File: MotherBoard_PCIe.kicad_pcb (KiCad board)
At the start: 2 copper layers, 90 x 100 mm, 27 parts, among them J1 Conn_01x02, J2 Conn_01x07, J3 Conn_01x02, J4 Conn_01x07, J5 Bus_PCIexpress_x16_164_Positi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, J6 Bus_PCIexpress_x16_164_Positi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, J7 Bus_PCIexpress_x16_164_Positi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, J8 Bus_PCIexpress_x16_164_Positi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, J9 Bus_mechaken_PCIexpress_x16_1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

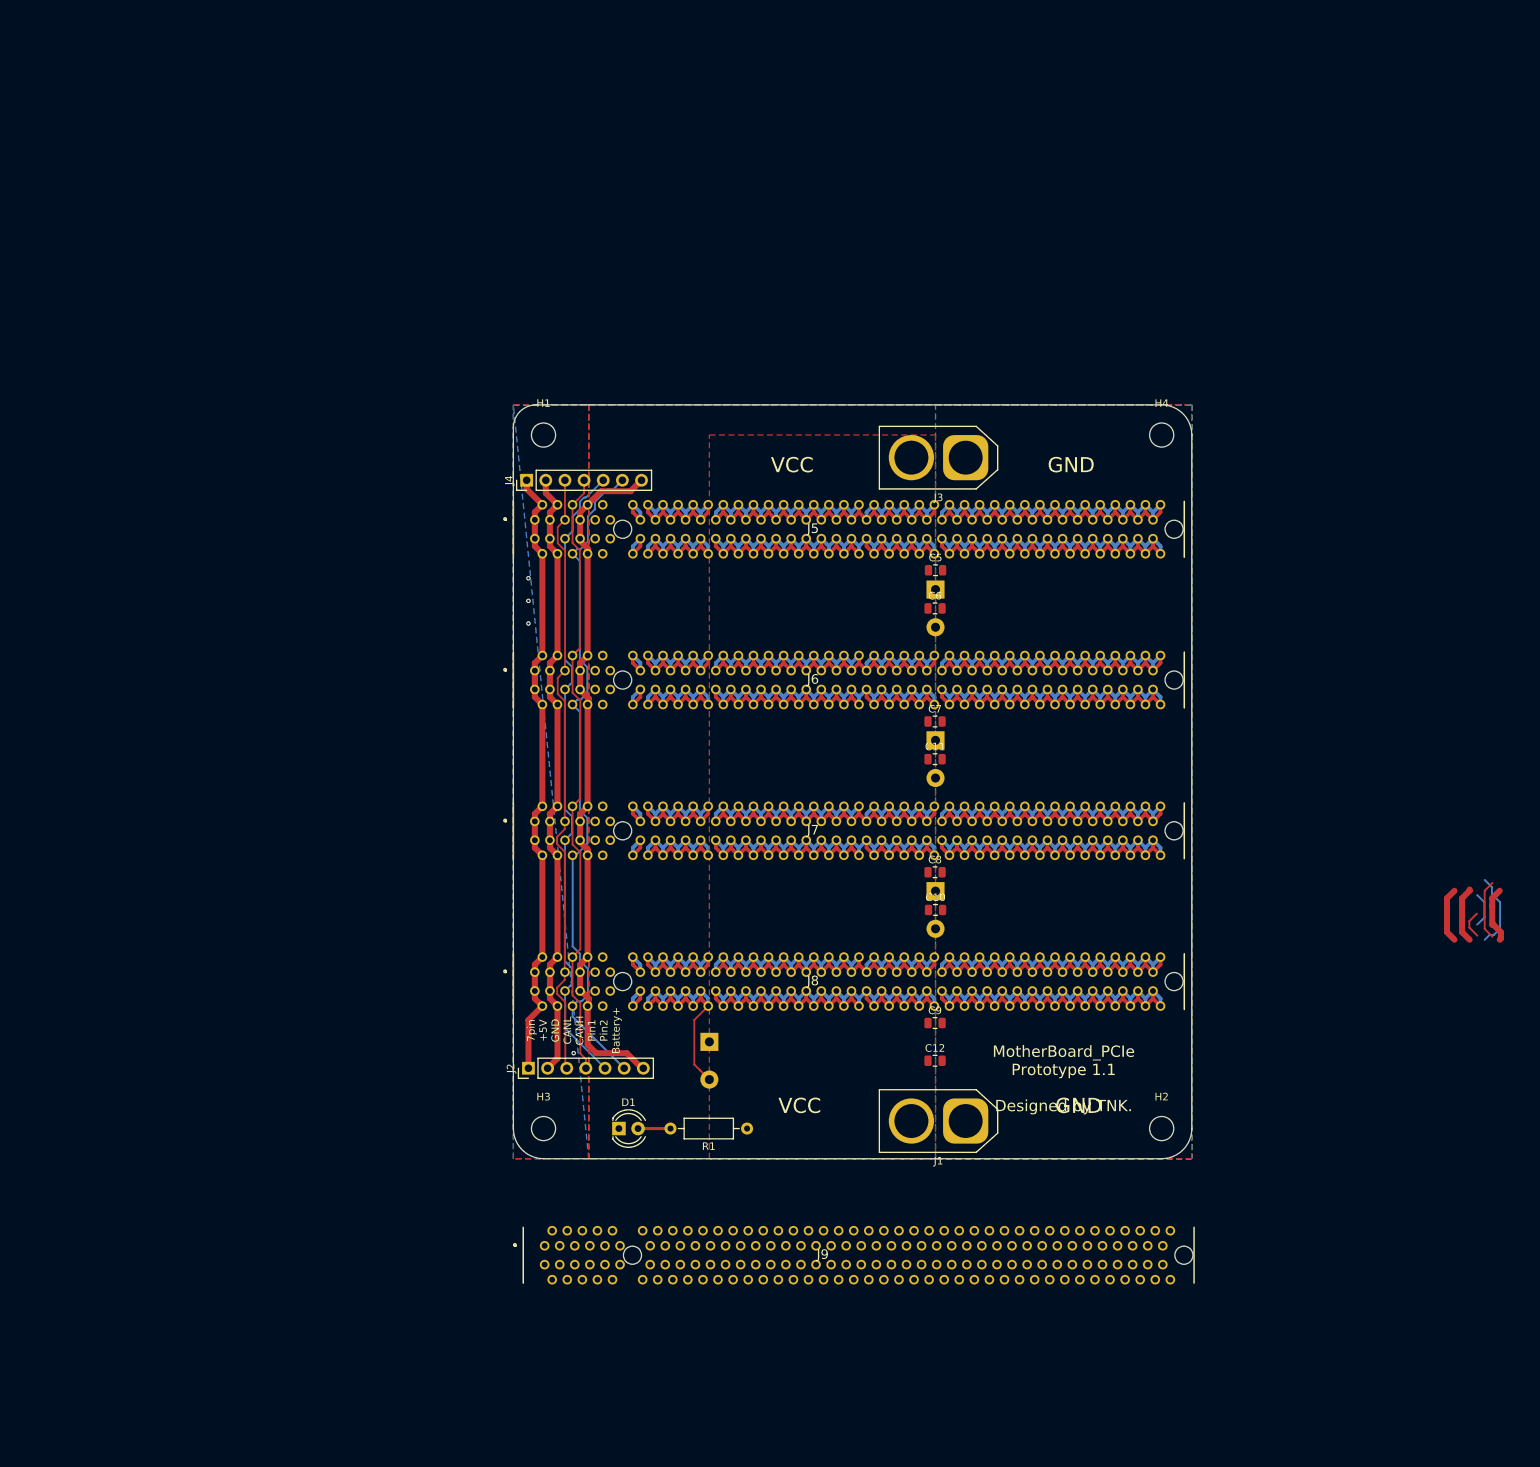
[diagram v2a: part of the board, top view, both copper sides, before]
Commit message: change
おおよその部品の配置を開始
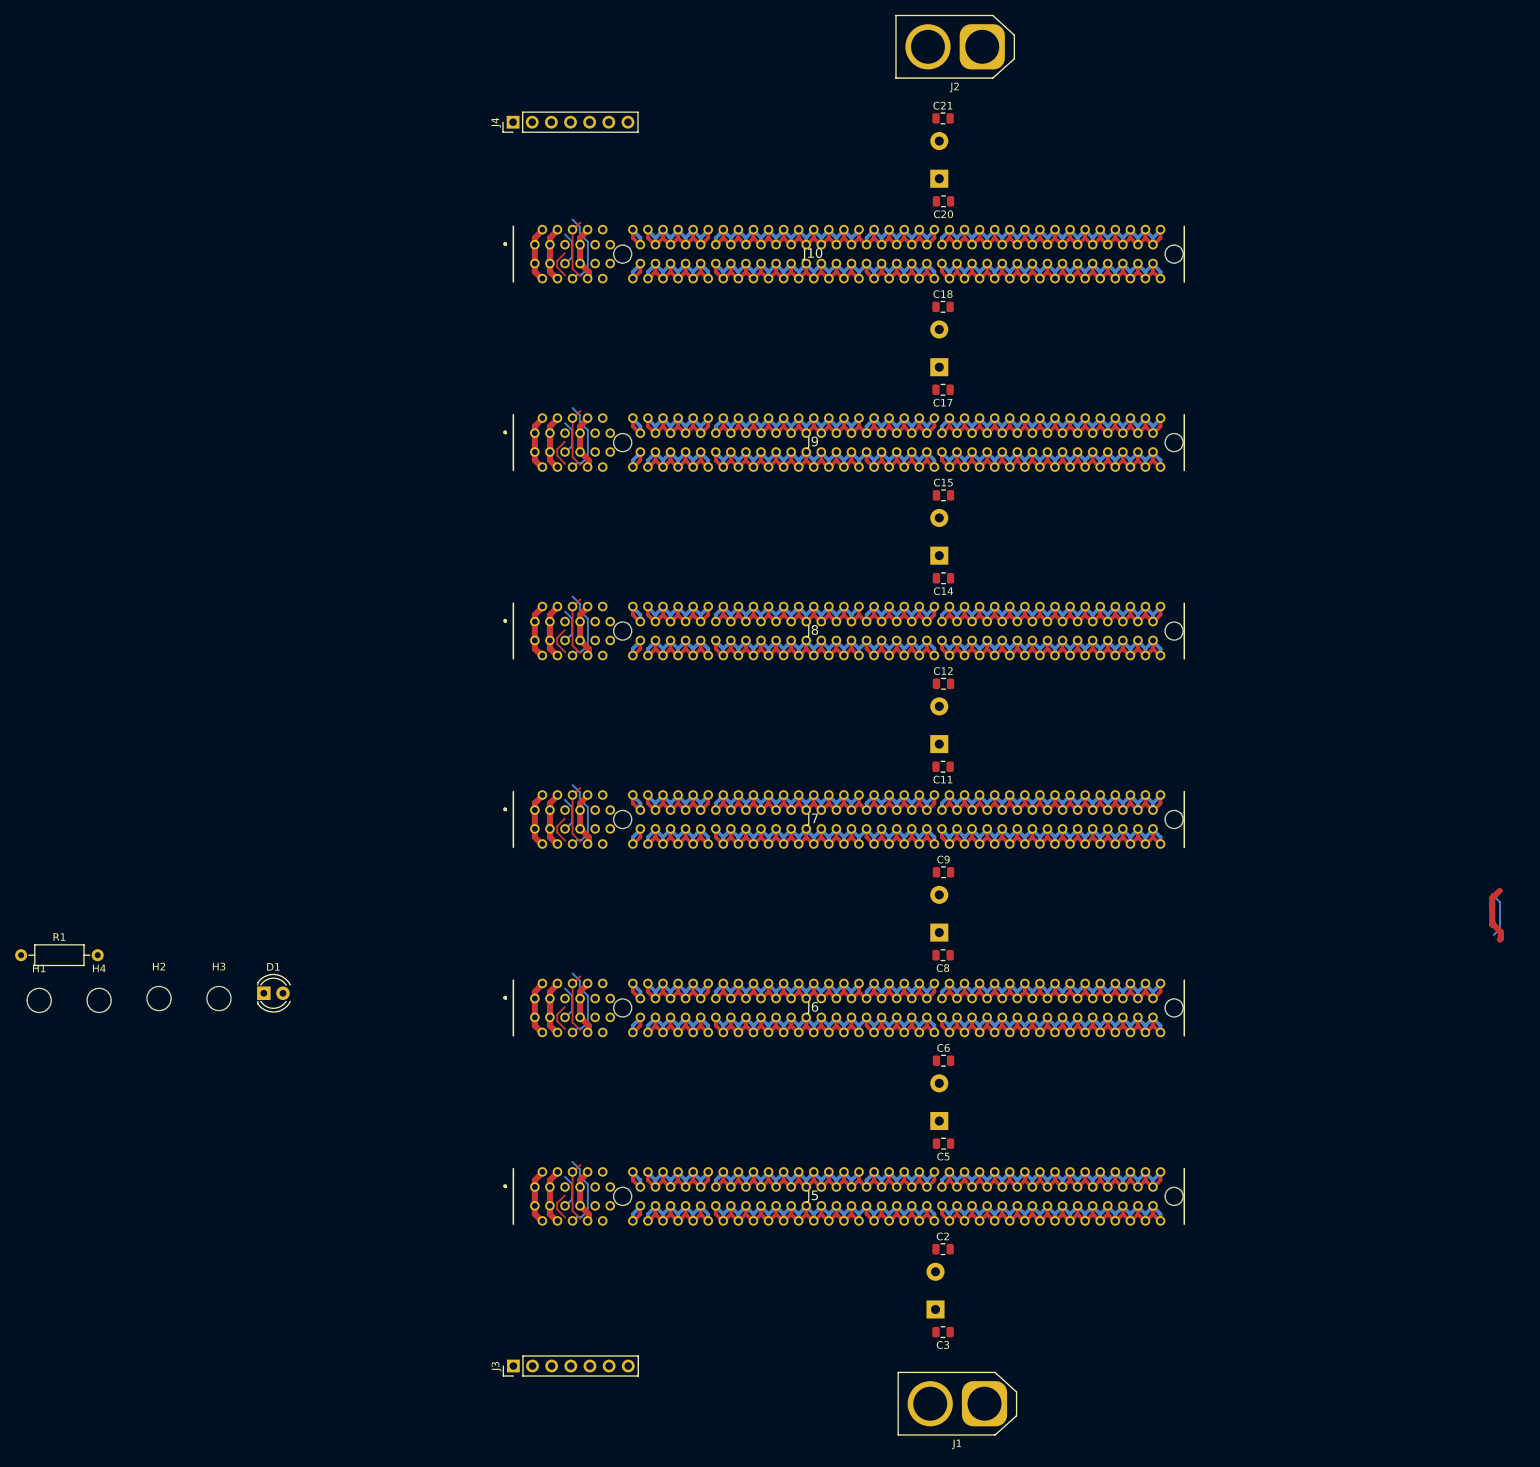
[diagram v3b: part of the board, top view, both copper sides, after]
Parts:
- added C13: 1000uF, Capacitor_THT:CP_Radial_D12.5mm_P5.00mm, B.Cu at (146.5, 85.0)
- added C14: 1uF, Capacitor_SMD:C_0805_2012Metric, F.Cu at (147.1, 88.0)
- added C15: 10uF, Capacitor_SMD:C_0805_2012Metric, F.Cu at (147.1, 77.0)
- added C16: 1000uF, Capacitor_THT:CP_Radial_D12.5mm_P5.00mm, B.Cu at (146.5, 60.0)
- added C17: 1uF, Capacitor_SMD:C_0805_2012Metric, F.Cu at (147.0, 63.0)
- added C18: 10uF, Capacitor_SMD:C_0805_2012Metric, F.Cu at (147.0, 52.0)
- added C19: 1000uF, Capacitor_THT:CP_Radial_D12.5mm_P5.00mm, B.Cu at (146.5, 35.0)
- added C20: 1uF, Capacitor_SMD:C_0805_2012Metric, F.Cu at (147.1, 38.0)
- added C21: 10uF, Capacitor_SMD:C_0805_2012Metric, F.Cu at (147.0, 27.0)
- added J10: Bus_mechaken_PCIexpress_x16_164_Position, PCIe:Socket_mechaken_PCIexpress_x16_164_position, F.Cu at (90.0, 45.0)
- C10: value 10uF -> 1000uF; footprint Capacitor_SMD:C_0805_2012Metric -> Capacitor_THT:CP_Radial_D12.5mm_P5.00mm; moved to B.Cu
- C11: value 10uF -> 1uF
- C2: value 1000uF -> 1uF; footprint Capacitor_THT:CP_Radial_D12.5mm_P5.00mm -> Capacitor_SMD:C_0805_2012Metric; moved to F.Cu
- C3: value 1000uF -> 10uF; footprint Capacitor_THT:CP_Radial_D12.5mm_P5.00mm -> Capacitor_SMD:C_0805_2012Metric; moved to F.Cu
- C7: value 1uF -> 1000uF; footprint Capacitor_SMD:C_0805_2012Metric -> Capacitor_THT:CP_Radial_D12.5mm_P5.00mm; moved to B.Cu
- C9: value 1uF -> 10uF
- J1: footprint Connector_AMASS:AMASS_XT60-F_1x02_P7.20mm_Vertical -> Connector_AMASS:AMASS_XT60-M_1x02_P7.20mm_Vertical
- J2: value Conn_01x07 -> Conn_01x02; footprint Connector_PinHeader_2.54mm:PinHeader_1x07_P2.54mm_Vertical -> Connector_AMASS:AMASS_XT60-F_1x02_P7.20mm_Vertical
- J3: value Conn_01x02 -> Conn_01x07; footprint Connector_AMASS:AMASS_XT60-M_1x02_P7.20mm_Vertical -> Connector_PinHeader_2.54mm:PinHeader_1x07_P2.54mm_Vertical
- J5, J6, J7, J8: value Bus_PCIexpress_x16_164_Position -> Bus_mechaken_PCIexpress_x16_164_Position; footprint SamacSys_Parts:10018783-10113TLF -> PCIe:Socket_mechaken_PCIexpress_x16_164_position
- moved H4 159.7 mm to (35.0, 144.0)
- moved J2 148.3 mm to (152.2, 17.5), turned to 180 degrees
- moved J3 134.6 mm to (90.0, 192.5), turned to 90 degrees
- moved H2 134.1 mm to (43.0, 143.8)
- moved J9 107.8 mm to (90.0, 70.0)
- moved H1 100.5 mm to (27.1, 144.0)
- moved R1 99.0 mm to (24.7, 138.0), turned to 0 degrees
- moved C3 98.5 mm to (147.0, 188.0), turned to 0 degrees
- moved J5 88.5 mm to (90.0, 170.0)
- moved C5 76.1 mm to (147.1, 163.0)
- moved C2 67.5 mm to (147.0, 177.0), turned to 0 degrees
- moved C6 60.0 mm to (147.1, 152.0)
- moved C1 55.5 mm to (146.0, 185.0), turned to 90 degrees
- moved D1 50.4 mm to (56.9, 143.1)
- moved C12 50.0 mm to (147.1, 102.0)
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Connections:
- J2 pad 1: +5V -> GNDPWR
- J2 pad 2: GND -> VCC
- J3 pad 1: GNDPWR -> +5V
- J3 pad 2: VCC -> GND
- J5 pad A10: VCC -> GNDPWR
- J5 pad A2: +5V -> GND
- J5 pad A3: GND -> CANL
- J5 pad A4: GND -> CANH
- J5 pad A5: CANL -> +BATT
- J5 pad A6: CANH -> VCC
- J5 pad A7: +BATT -> VCC
- J5 pad A8: +BATT -> GNDPWR
- J5 pad B10: VCC -> GNDPWR
- J5 pad B2: +5V -> GND
- J5 pad B3: GND -> Pin_B5
- J5 pad B4: GND -> Pin_B6
- J5 pad B5: Pin_B5 -> +BATT
- J5 pad B6: Pin_B6 -> VCC
- J5 pad B7: +BATT -> VCC
- J5 pad B8: +BATT -> GNDPWR
- J6 pad A10: VCC -> GNDPWR
- J6 pad A2: +5V -> GND
- J6 pad A3: GND -> CANL
- J6 pad A4: GND -> CANH
- J6 pad A5: CANL -> +BATT
- J6 pad A6: CANH -> VCC
- J6 pad A7: +BATT -> VCC
- J6 pad A8: +BATT -> GNDPWR
- J6 pad B10: VCC -> GNDPWR
- J6 pad B2: +5V -> GND
- J6 pad B3: GND -> Pin_B5
- J6 pad B4: GND -> Pin_B6
- J6 pad B5: Pin_B5 -> +BATT
- J6 pad B6: Pin_B6 -> VCC
- J6 pad B7: +BATT -> VCC
- J6 pad B8: +BATT -> GNDPWR
- J7 pad A10: VCC -> GNDPWR
- J7 pad A2: +5V -> GND
- J7 pad A3: GND -> CANL
- J7 pad A4: GND -> CANH
- J7 pad A5: CANL -> +BATT
- J7 pad A6: CANH -> VCC
- J7 pad A7: +BATT -> VCC
- J7 pad A8: +BATT -> GNDPWR
- J7 pad B10: VCC -> GNDPWR
- J7 pad B2: +5V -> GND
- J7 pad B3: GND -> Pin_B5
- J7 pad B4: GND -> Pin_B6
- J7 pad B5: Pin_B5 -> +BATT
- J7 pad B6: Pin_B6 -> VCC
- J7 pad B7: +BATT -> VCC
- J7 pad B8: +BATT -> GNDPWR
- J8 pad A10: VCC -> GNDPWR
- J8 pad A2: +5V -> GND
- J8 pad A3: GND -> CANL
- J8 pad A4: GND -> CANH
- J8 pad A5: CANL -> +BATT
- J8 pad A6: CANH -> VCC
- J8 pad A7: +BATT -> VCC
- J8 pad A8: +BATT -> GNDPWR
- J8 pad B10: VCC -> GNDPWR
- J8 pad B2: +5V -> GND
- J8 pad B3: GND -> Pin_B5
- J8 pad B4: GND -> Pin_B6
- J8 pad B5: Pin_B5 -> +BATT
- J8 pad B6: Pin_B6 -> VCC
- J8 pad B7: +BATT -> VCC
- J8 pad B8: +BATT -> GNDPWR
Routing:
- net GNDPWR: track 1160.6 -> 1723.8 mm
- net VCC: track 923.5 -> 1385.3 mm
- net Pin_B4: track 84.8 -> 0.00 mm
- net CANL: track 81.4 -> 0.00 mm
- net Pin_B5: track 90.1 -> 28.4 mm
- net Pin_B6: track 0.00 -> 59.7 mm
- net +BATT: track 92.4 -> 45.2 mm
- net +5V: track 82.9 -> 44.0 mm
- net GND: track 82.5 -> 45.0 mm, vias 4 -> 0
- net CANH: track 81.9 -> 48.0 mm
- net (no net): track 567.0 -> 554.6 mm
- net Net-(D1-Pad2): track 4.30 -> 0.00 mm
- removed copper zone on B.Cu, net GND
- removed copper zone on F.Cu, net GND
- removed copper zone on B.Cu, net GNDPWR
- removed copper zone on F.Cu, net GNDPWR
- removed copper zone on B.Cu, net VCC
- removed copper zone on F.Cu, net VCC
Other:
- board outline removed
- board text removed: "7pin +5V GND CANL CANH Pin1 Pin2 Battery+"
- board text removed: "Designed by TNK."
- board text removed: "GND"
- board text removed: "MotherBoard_PCIe Prototype 1.1"
- board text removed: "VCC"

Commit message: add
いったん完成
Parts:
- moved H3 161.0 mm to (142.0, 11.0)
- moved H1 137.5 mm to (62.0, 11.0)
- moved H4 118.9 mm to (142.0, 196.0)
- moved R1 83.4 mm to (87.0, 193.5), turned to 180 degrees
- moved D1 61.4 mm to (92.0, 193.5)
- moved H2 55.6 mm to (62.0, 196.0)
- moved C1 33.6 mm to (113.0, 178.5)
- moved C10 33.6 mm to (113.5, 103.5)
- moved C11 33.6 mm to (114.0, 106.5)
- moved C12 33.6 mm to (114.1, 95.5)
- moved C13 33.6 mm to (113.5, 78.5)
- moved C14 33.6 mm to (114.1, 81.5)
- moved C15 33.6 mm to (114.1, 70.5)
- moved C16 33.6 mm to (113.5, 53.5)
- moved C17 33.6 mm to (114.0, 56.5)
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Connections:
- D1 pad 1: GNDPWR -> Net-(D1-Pad1)
- D1 pad 2: Net-(D1-Pad2) -> VCC
- J3 pad 5: Pin_B4 -> Pin_B5
- J3 pad 6: Pin_B5 -> Pin_B6
- J4 pad 5: Pin_B4 -> Pin_B5
- J4 pad 6: Pin_B5 -> Pin_B6
- R1 pad 1: VCC -> Net-(D1-Pad1)
- R1 pad 2: Net-(D1-Pad2) -> GNDPWR
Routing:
- net (no net): track 554.6 -> 0.00 mm
- net CANL: track 0.00 -> 166.4 mm
- net Pin_B5: track 28.4 -> 174.3 mm
- net VCC: track 1385.3 -> 1529.7 mm, vias 0 -> 210
- net +BATT: track 45.2 -> 179.2 mm
- net GND: track 45.0 -> 171.7 mm, vias 0 -> 52
- net Pin_B6: track 59.7 -> 183.4 mm
- net +5V: track 44.0 -> 167.1 mm
- net CANH: track 48.0 -> 168.4 mm
- net GNDPWR: track 1723.8 -> 1749.3 mm, vias 0 -> 250
- net Net-(D1-Pad1): track 0.00 -> 4.96 mm
- added copper zone on B.Cu, net GND
- added copper zone on F.Cu, net GND
- added copper zone on B.Cu, net GNDPWR
- added copper zone on F.Cu, net GNDPWR
- added copper zone on B.Cu, net VCC
- added copper zone on F.Cu, net VCC
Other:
- board outline added: 90 x 196 mm
- board text added: "+5V GND CANL CANH Pin_B5 Pin_B6 +BATT"
- board text added: "Back"
- board text added: "C1, C4, C7, C10, C13, C16, C19 -> 1000uF C2, C5, C8, C11, C14, C17, C20 -> 10uF C3, C6, C9, C12, C15, C18, C21 -> 1uF"
- board text added: "Front"
- board text added: "GND"
- board text added: "Input"
- board text added: "Motherboard PCIe x16 Prototype 1.1 Designed by TNK."
- board text added: "Output"
- board text added: "VCC"

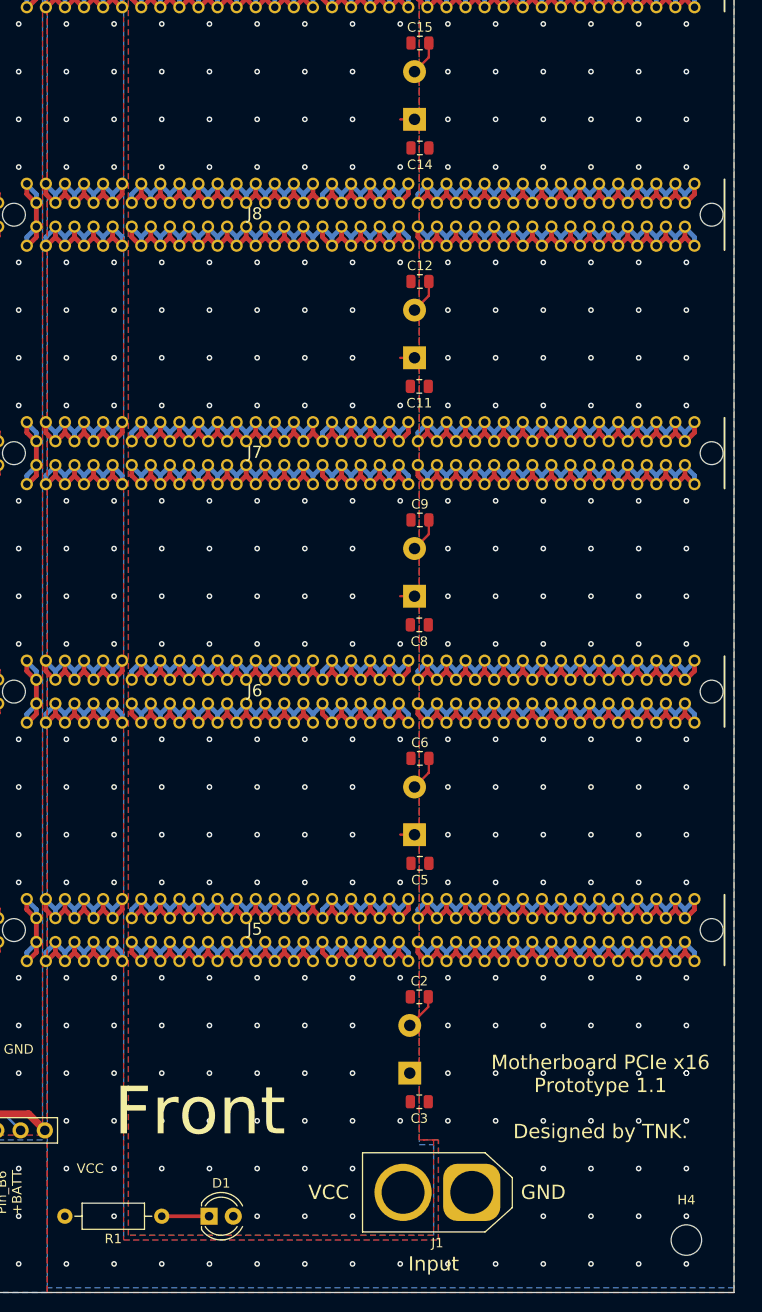
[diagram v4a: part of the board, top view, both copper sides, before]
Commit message: add
3ピンファンコネクタを追加
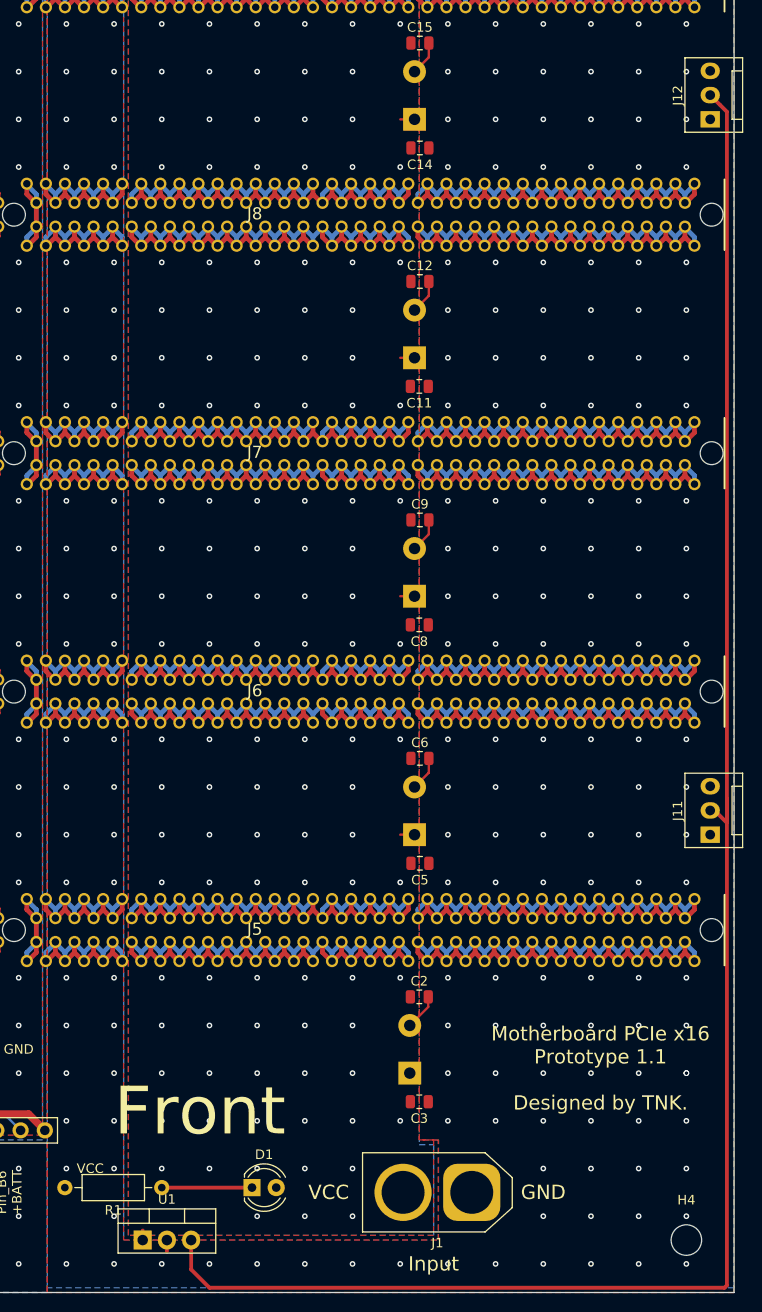
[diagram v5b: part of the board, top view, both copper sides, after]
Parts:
- added J11: Conn_01x03, Connector:FanPinHeader_1x03_P2.54mm_Vertical, F.Cu at (144.5, 153.5)
- added J12: Conn_01x03, Connector:FanPinHeader_1x03_P2.54mm_Vertical, F.Cu at (144.5, 78.5)
- added U1: L7812, Package_TO_SOT_THT:TO-220-3_Vertical, F.Cu at (85.0, 196.0)
- moved D1 5.41 mm to (96.5, 190.5)
- moved R1 3.00 mm to (87.0, 190.5)
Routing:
- net +12V: track 0.00 -> 190.4 mm
- net Net-(D1-Pad1): track 4.96 -> 9.46 mm
- net GNDPWR: track 1749.3 -> 1750.5 mm
- net VCC: track 1529.7 -> 1530.7 mm
